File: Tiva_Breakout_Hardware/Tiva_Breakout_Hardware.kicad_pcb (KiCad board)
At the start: 2 copper layers, 146.1 x 69.8 mm, 15 parts, among them U1 TM4C129E_Launchpad

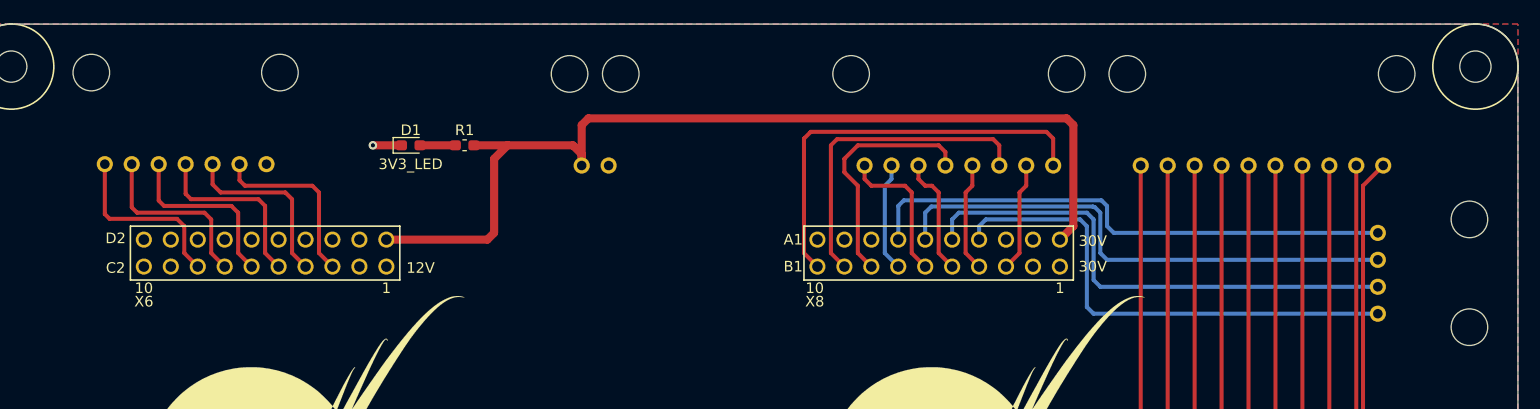
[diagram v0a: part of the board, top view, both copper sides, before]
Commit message: Finished 30V LEDs and connectors
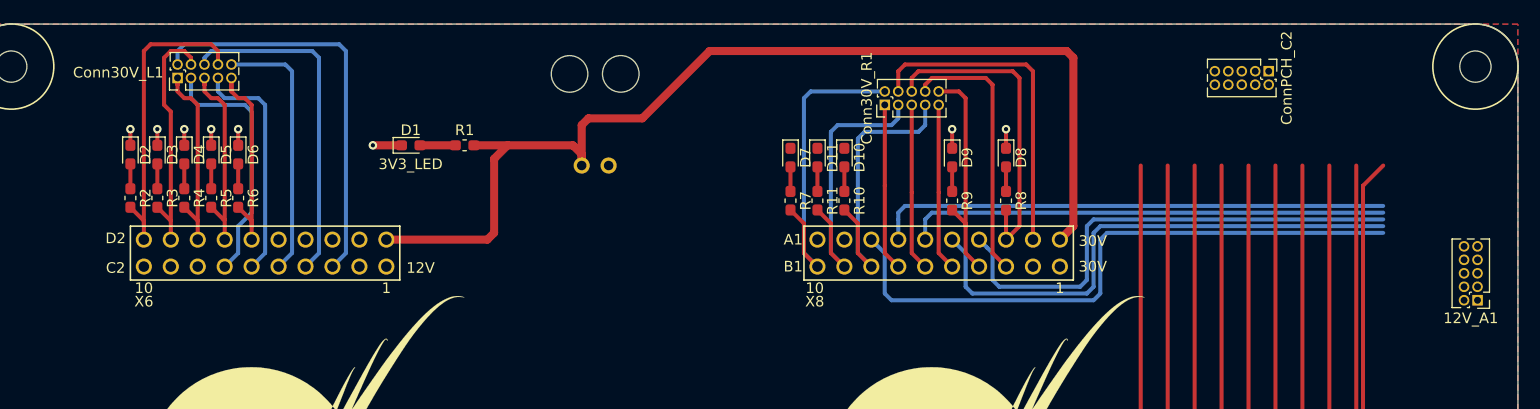
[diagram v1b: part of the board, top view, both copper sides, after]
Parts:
- removed 12V_B2: Molex_SL_04, MRDT_Connectors:MOLEX_SL_04_Horizontal
- added 12V_A1: PH_2x5, Connector_PinHeader_1.27mm:PinHeader_2x05_P1.27mm_Vertical, F.Cu at (226.8, 101.3)
- added D10: 3V3_LED, LED_SMD:LED_0603_1608Metric_Pad1.05x0.95mm_HandSolder, F.Cu at (167.1, 87.9)
- added D11: 3V3_LED, LED_SMD:LED_0603_1608Metric_Pad1.05x0.95mm_HandSolder, F.Cu at (164.5, 87.9)
- added D2: 3V3_LED, LED_SMD:LED_0603_1608Metric_Pad1.05x0.95mm_HandSolder, F.Cu at (99.8, 87.6)
- added D3: 3V3_LED, LED_SMD:LED_0603_1608Metric_Pad1.05x0.95mm_HandSolder, F.Cu at (102.3, 87.6)
- added D4: 3V3_LED, LED_SMD:LED_0603_1608Metric_Pad1.05x0.95mm_HandSolder, F.Cu at (104.9, 87.6)
- added D5: 3V3_LED, LED_SMD:LED_0603_1608Metric_Pad1.05x0.95mm_HandSolder, F.Cu at (107.4, 87.6)
- added D6: 3V3_LED, LED_SMD:LED_0603_1608Metric_Pad1.05x0.95mm_HandSolder, F.Cu at (109.9, 87.6)
- added D7: 3V3_LED, LED_SMD:LED_0603_1608Metric_Pad1.05x0.95mm_HandSolder, F.Cu at (162.0, 87.9)
- added D8: 3V3_LED, LED_SMD:LED_0603_1608Metric_Pad1.05x0.95mm_HandSolder, F.Cu at (182.3, 87.9)
- added D9: 3V3_LED, LED_SMD:LED_0603_1608Metric_Pad1.05x0.95mm_HandSolder, F.Cu at (177.2, 87.9)
- added R10: 330, Resistor_SMD:R_0603_1608Metric_Pad1.05x0.95mm_HandSolder, F.Cu at (167.1, 92.0)
- added R11: 330, Resistor_SMD:R_0603_1608Metric_Pad1.05x0.95mm_HandSolder, F.Cu at (164.5, 92.0)
- added R2: 330, Resistor_SMD:R_0603_1608Metric_Pad1.05x0.95mm_HandSolder, F.Cu at (99.8, 91.7)
- added R3: 330, Resistor_SMD:R_0603_1608Metric_Pad1.05x0.95mm_HandSolder, F.Cu at (102.3, 91.7)
- added R4: 330, Resistor_SMD:R_0603_1608Metric_Pad1.05x0.95mm_HandSolder, F.Cu at (104.9, 91.7)
- added R5: 330, Resistor_SMD:R_0603_1608Metric_Pad1.05x0.95mm_HandSolder, F.Cu at (107.4, 91.7)
- added R6: 330, Resistor_SMD:R_0603_1608Metric_Pad1.05x0.95mm_HandSolder, F.Cu at (109.9, 91.7)
- added R7: 330, Resistor_SMD:R_0603_1608Metric_Pad1.05x0.95mm_HandSolder, F.Cu at (162.0, 92.0)
- added R8: 330, Resistor_SMD:R_0603_1608Metric_Pad1.05x0.95mm_HandSolder, F.Cu at (182.3, 92.0)
- added R9: 330, Resistor_SMD:R_0603_1608Metric_Pad1.05x0.95mm_HandSolder, F.Cu at (177.2, 92.0)
- Conn30V_L1: value Molex_SL_07 -> PH_2x5; footprint MRDT_Connectors:MOLEX_SL_07_Horizontal -> Connector_PinHeader_1.27mm:PinHeader_2x05_P1.27mm_Vertical; moved to F.Cu
- Conn30V_R1: value Molex_SL_08 -> PH_2x5; footprint MRDT_Connectors:MOLEX_SL_08_Horizontal -> Connector_PinHeader_1.27mm:PinHeader_2x05_P1.27mm_Vertical; moved to F.Cu
- ConnPCH_C2: value Molex_SL_10 -> PH_2x5; footprint MRDT_Connectors:MOLEX_SL_10_Horizontal -> Connector_PinHeader_1.27mm:PinHeader_2x05_P1.27mm_Vertical; moved to F.Cu
- moved Conn30V_R1 9.03 mm to (170.9, 82.9), turned to 90 degrees
- moved ConnPCH_C2 8.91 mm to (207.1, 79.8), turned to 270 degrees
- moved Conn30V_L1 8.16 mm to (104.2, 80.4), turned to 90 degrees
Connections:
- net 12V_ON renamed M6_EN
- net Net-(Conn30V_L1-Pad2) renamed M3_ISENSE
- Conn30V_L1 pad 1: Net-(Conn30V_L1-Pad1) -> M3_EN
- Conn30V_L1 pad 3: Net-(Conn30V_L1-Pad3) -> M4_ISENSE
- Conn30V_L1 pad 4: Net-(Conn30V_L1-Pad4) -> M2_EN
- Conn30V_L1 pad 5: Net-(Conn30V_L1-Pad5) -> M4_EN
- Conn30V_L1 pad 6: Net-(Conn30V_L1-Pad6) -> M2_ISENSE
- Conn30V_L1 pad 7: Net-(Conn30V_L1-Pad7) -> M5_ISENSE
- Conn30V_R1 pad 1: EX_ON -> M6_ISENSE
- Conn30V_R1 pad 2: EX_CURR -> RKT_EN
- Conn30V_R1 pad 4: 12V_CURR -> RKT_ISENSE
- Conn30V_R1 pad 5: AUX_ON -> SP_ISENSE
- Conn30V_R1 pad 6: AUX_CURR -> AUX_EN
- Conn30V_R1 pad 7: RKT_ON -> SP_EN
- Conn30V_R1 pad 8: RKT_CURR -> AUX_ISENSE
- U1 pad PA6: AUX_ON -> SP_EN
- U1 pad PB5: Net-(Conn30V_L1-Pad3) -> M2_ISENSE
- U1 pad PC4: Net-(U1-PadPC4) -> AUX_EN
- U1 pad PD5: Net-(U1-PadPD5) -> M5_EN
- U1 pad PD7: RKT_ON -> M6_ISENSE
- U1 pad PE0: EX_CURR -> AUX_ISENSE
- U1 pad PE1: 12V_CURR -> 12V_EN
- U1 pad PE2: AUX_CURR -> 12V_ISENSE
- U1 pad PE3: RKT_CURR -> SP_ISENSE
- U1 pad PE4: Net-(U1-PadPE4) -> RKT_ISENSE
- U1 pad PF1: Net-(ConnPCH_C2-Pad1) -> Net-(U1-PadPF1)
- U1 pad PF2: Net-(ConnPCH_C2-Pad2) -> Net-(U1-PadPF2)
- U1 pad PF3: Net-(ConnPCH_C2-Pad3) -> Net-(U1-PadPF3)
- U1 pad PG0: Net-(ConnPCH_C2-Pad4) -> Net-(U1-PadPG0)
- U1 pad PK0: Net-(Conn30V_L1-Pad4) -> M1_ISENSE
- U1 pad PK1: Net-(Conn30V_L1-Pad5) -> M5_ISENSE
- U1 pad PK2: Net-(Conn30V_L1-Pad6) -> M4_ISENSE
- U1 pad PK3: Net-(Conn30V_L1-Pad7) -> Net-(U1-PadPK3)
- U1 pad PL0: Net-(ConnPCH_C2-Pad7) -> Net-(U1-PadPL0)
- U1 pad PL1: Net-(ConnPCH_C2-Pad8) -> Net-(U1-PadPL1)
- U1 pad PL2: Net-(ConnPCH_C2-Pad9) -> Net-(U1-PadPL2)
- U1 pad PL3: Net-(ConnPCH_C2-Pad10) -> Net-(U1-PadPL3)
- U1 pad PL4: Net-(ConnPCH_C2-Pad5) -> Net-(U1-PadPL4)
- U1 pad PL5: Net-(ConnPCH_C2-Pad6) -> Net-(U1-PadPL5)
- U1 pad PM5: EX_ON -> RKT_EN
- U1 pad PN4: Net-(U1-PadPN4) -> M1_EN
- U1 pad PN5: Net-(U1-PadPN5) -> M2_EN
- U1 pad PP4: Net-(U1-PadPP4) -> M3_EN
- U1 pad PQ0: Net-(U1-PadPQ0) -> M4_EN
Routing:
- net Net-(U1-PadPL3): track 0.00 -> 79.9 mm
- net Net-(U1-PadPL2): track 0.00 -> 79.9 mm
- net Net-(U1-PadPL0): track 0.00 -> 79.9 mm
- net Net-(U1-PadPG0): track 0.00 -> 79.9 mm
- net Net-(U1-PadPF3): track 0.00 -> 79.9 mm
- net Net-(ConnPCH_C2-Pad9): track 79.9 -> 0.00 mm
- net Net-(ConnPCH_C2-Pad7): track 79.9 -> 0.00 mm
- net Net-(ConnPCH_C2-Pad4): track 79.9 -> 0.00 mm
- net Net-(ConnPCH_C2-Pad3): track 79.9 -> 0.00 mm
- net Net-(ConnPCH_C2-Pad10): track 79.9 -> 0.00 mm
- net Net-(U1-PadPL5): track 0.00 -> 79.9 mm
- net Net-(U1-PadPL4): track 0.00 -> 79.9 mm
- net Net-(U1-PadPL1): track 0.00 -> 79.9 mm
- net Net-(ConnPCH_C2-Pad8): track 79.9 -> 0.00 mm
- net Net-(ConnPCH_C2-Pad6): track 79.9 -> 0.00 mm
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
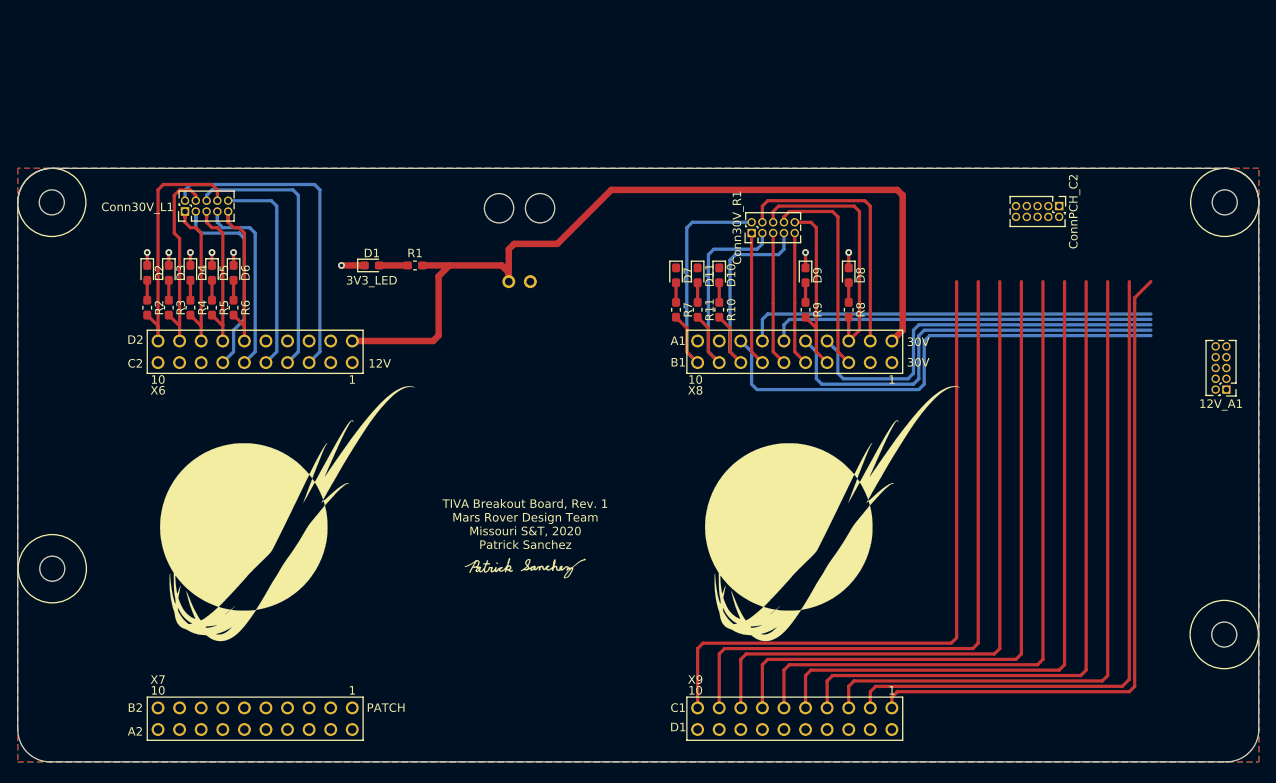
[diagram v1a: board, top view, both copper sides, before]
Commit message: Rerouted 30V for readability; routed 12V and LEDs
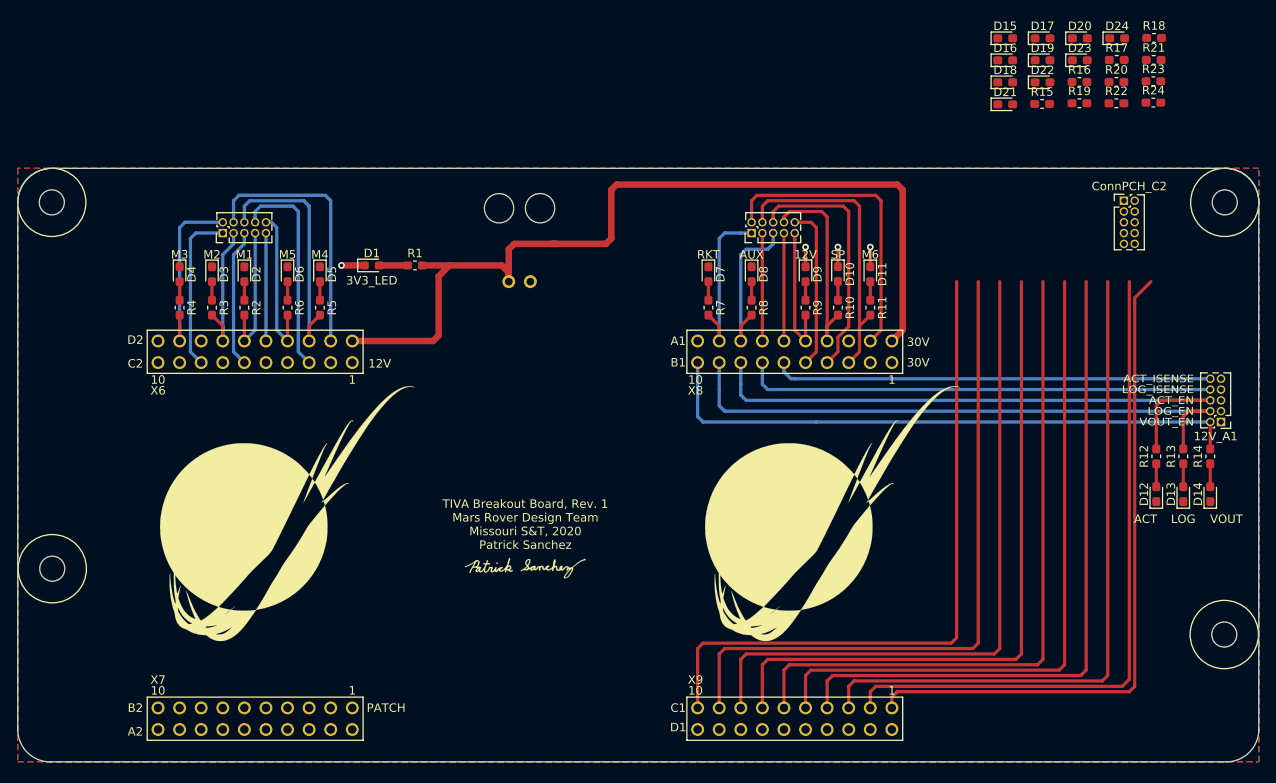
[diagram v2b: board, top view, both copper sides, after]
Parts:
- added D12: 3V3_LED, LED_SMD:LED_0603_1608Metric_Pad1.05x0.95mm_HandSolder, F.Cu at (218.5, 113.7)
- added D13: 3V3_LED, LED_SMD:LED_0603_1608Metric_Pad1.05x0.95mm_HandSolder, F.Cu at (221.7, 113.7)
- added D14: 3V3_LED, LED_SMD:LED_0603_1608Metric_Pad1.05x0.95mm_HandSolder, F.Cu at (224.9, 113.7)
- added D15: 3V3_LED, LED_SMD:LED_0603_1608Metric_Pad1.05x0.95mm_HandSolder, F.Cu at (200.7, 60.0)
- added D16: 3V3_LED, LED_SMD:LED_0603_1608Metric_Pad1.05x0.95mm_HandSolder, F.Cu at (200.7, 62.6)
- added D17: 3V3_LED, LED_SMD:LED_0603_1608Metric_Pad1.05x0.95mm_HandSolder, F.Cu at (205.1, 60.0)
- added D18: 3V3_LED, LED_SMD:LED_0603_1608Metric_Pad1.05x0.95mm_HandSolder, F.Cu at (200.7, 65.2)
- added D19: 3V3_LED, LED_SMD:LED_0603_1608Metric_Pad1.05x0.95mm_HandSolder, F.Cu at (205.1, 62.6)
- added D20: 3V3_LED, LED_SMD:LED_0603_1608Metric_Pad1.05x0.95mm_HandSolder, F.Cu at (209.5, 60.0)
- added D21: 3V3_LED, LED_SMD:LED_0603_1608Metric_Pad1.05x0.95mm_HandSolder, F.Cu at (200.7, 67.8)
- added D22: 3V3_LED, LED_SMD:LED_0603_1608Metric_Pad1.05x0.95mm_HandSolder, F.Cu at (205.1, 65.2)
- added D23: 3V3_LED, LED_SMD:LED_0603_1608Metric_Pad1.05x0.95mm_HandSolder, F.Cu at (209.5, 62.6)
- added D24: 3V3_LED, LED_SMD:LED_0603_1608Metric_Pad1.05x0.95mm_HandSolder, F.Cu at (213.9, 60.0)
- added R12: 330, Resistor_SMD:R_0603_1608Metric_Pad1.05x0.95mm_HandSolder, F.Cu at (218.5, 109.2)
- added R13: 330, Resistor_SMD:R_0603_1608Metric_Pad1.05x0.95mm_HandSolder, F.Cu at (221.7, 109.2)
- added R14: 330, Resistor_SMD:R_0603_1608Metric_Pad1.05x0.95mm_HandSolder, F.Cu at (224.9, 109.2)
- added R15: 330, Resistor_SMD:R_0603_1608Metric_Pad1.05x0.95mm_HandSolder, F.Cu at (205.1, 67.7)
- added R16: 330, Resistor_SMD:R_0603_1608Metric_Pad1.05x0.95mm_HandSolder, F.Cu at (209.5, 65.1)
- added R17: 330, Resistor_SMD:R_0603_1608Metric_Pad1.05x0.95mm_HandSolder, F.Cu at (213.9, 62.6)
- added R18: 330, Resistor_SMD:R_0603_1608Metric_Pad1.05x0.95mm_HandSolder, F.Cu at (218.3, 60.0)
- added R19: 330, Resistor_SMD:R_0603_1608Metric_Pad1.05x0.95mm_HandSolder, F.Cu at (209.5, 67.7)
- added R20: 330, Resistor_SMD:R_0603_1608Metric_Pad1.05x0.95mm_HandSolder, F.Cu at (213.8, 65.1)
- added R21: 330, Resistor_SMD:R_0603_1608Metric_Pad1.05x0.95mm_HandSolder, F.Cu at (218.2, 62.6)
- added R22: 330, Resistor_SMD:R_0603_1608Metric_Pad1.05x0.95mm_HandSolder, F.Cu at (213.8, 67.7)
- added R23: 330, Resistor_SMD:R_0603_1608Metric_Pad1.05x0.95mm_HandSolder, F.Cu at (218.2, 65.1)
- added R24: 330, Resistor_SMD:R_0603_1608Metric_Pad1.05x0.95mm_HandSolder, F.Cu at (218.2, 67.6)
- moved R11 20.3 mm to (184.9, 91.7)
- moved D11 20.3 mm to (184.9, 87.8)
- moved R10 14.0 mm to (181.1, 91.7)
- moved D10 14.0 mm to (181.1, 87.8)
- moved D5 12.7 mm to (120.1, 87.8)
- moved R5 12.7 mm to (120.1, 91.7)
- moved R8 11.4 mm to (170.9, 91.7)
- moved D2 11.4 mm to (111.2, 87.8)
- moved D8 11.4 mm to (170.9, 87.8)
- moved R2 11.4 mm to (111.2, 91.7)
- moved ConnPCH_C2 7.65 mm to (214.7, 79.1), turned to 0 degrees
- moved D6 6.35 mm to (116.3, 87.8)
- moved R6 6.35 mm to (116.3, 91.7)
- moved Conn30V_L1 5.12 mm to (108.7, 82.9)
- moved D3 5.08 mm to (107.4, 87.8)
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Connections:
- 12V_A1 pad 1: Net-(12V_A1-Pad1) -> GND
- 12V_A1 pad 10: Net-(12V_A1-Pad10) -> ACT_ISENSE
- 12V_A1 pad 2: Net-(12V_A1-Pad2) -> VOUT_EN
- 12V_A1 pad 3: Net-(12V_A1-Pad3) -> GND
- 12V_A1 pad 4: Net-(12V_A1-Pad4) -> LOG_EN
- 12V_A1 pad 5: Net-(12V_A1-Pad5) -> GND
- 12V_A1 pad 6: Net-(12V_A1-Pad6) -> ACT_EN
- 12V_A1 pad 7: Net-(12V_A1-Pad7) -> GND
- 12V_A1 pad 8: Net-(12V_A1-Pad8) -> LOG_ISENSE
- 12V_A1 pad 9: Net-(12V_A1-Pad9) -> GND
- Conn30V_L1 pad 1: M3_EN -> M3_ISENSE
- Conn30V_L1 pad 10: M1_ISENSE -> M5_EN
- Conn30V_L1 pad 2: M3_ISENSE -> M3_EN
- Conn30V_L1 pad 3: M4_ISENSE -> M2_EN
- Conn30V_L1 pad 4: M2_EN -> M4_ISENSE
- Conn30V_L1 pad 5: M4_EN -> M2_ISENSE
- Conn30V_L1 pad 6: M2_ISENSE -> M4_EN
- Conn30V_L1 pad 7: M5_ISENSE -> M1_EN
- Conn30V_L1 pad 8: M1_EN -> M5_ISENSE
- Conn30V_L1 pad 9: M5_EN -> M1_ISENSE
- Conn30V_R1 pad 1: M6_ISENSE -> RKT_EN
- Conn30V_R1 pad 10: 12V_EN -> 12V_ISENSE
- Conn30V_R1 pad 2: RKT_EN -> M6_ISENSE
- Conn30V_R1 pad 3: M6_EN -> RKT_ISENSE
- Conn30V_R1 pad 4: RKT_ISENSE -> M6_EN
- Conn30V_R1 pad 5: SP_ISENSE -> AUX_EN
- Conn30V_R1 pad 6: AUX_EN -> SP_ISENSE
- Conn30V_R1 pad 7: SP_EN -> AUX_ISENSE
- Conn30V_R1 pad 8: AUX_ISENSE -> SP_EN
- Conn30V_R1 pad 9: 12V_ISENSE -> 12V_EN
- ConnPCH_C2 pad 1: Net-(ConnPCH_C2-Pad1) -> PATCH10_EN
- ConnPCH_C2 pad 10: Net-(ConnPCH_C2-Pad10) -> PATCH5_EN
- ConnPCH_C2 pad 2: Net-(ConnPCH_C2-Pad2) -> PATCH1_EN
- ConnPCH_C2 pad 3: Net-(ConnPCH_C2-Pad3) -> PATCH9_EN
- ConnPCH_C2 pad 4: Net-(ConnPCH_C2-Pad4) -> PATCH2_EN
- ConnPCH_C2 pad 5: Net-(ConnPCH_C2-Pad5) -> PATCH8_EN
- ConnPCH_C2 pad 6: Net-(ConnPCH_C2-Pad6) -> PATCH3_EN
- ConnPCH_C2 pad 7: Net-(ConnPCH_C2-Pad7) -> PATCH7_EN
- ConnPCH_C2 pad 8: Net-(ConnPCH_C2-Pad8) -> PATCH4_EN
- ConnPCH_C2 pad 9: Net-(ConnPCH_C2-Pad9) -> PATCH6_EN
- U1 pad PA6: SP_EN -> ACT_EN
- U1 pad PB2: Net-(U1-PadPB2) -> RKT_EN
- U1 pad PB4: M3_ISENSE -> M5_ISENSE
- U1 pad PB5: M2_ISENSE -> Net-(U1-PadPB5)
- U1 pad PC4: AUX_EN -> Net-(U1-PadPC4)
- U1 pad PC5: Net-(U1-PadPC5) -> SP_EN
- U1 pad PC6: Net-(U1-PadPC6) -> 12V_EN
- U1 pad PC7: Net-(U1-PadPC7) -> AUX_EN
- U1 pad PD2: Net-(U1-PadPD2) -> M4_ISENSE
- U1 pad PD3: Net-(U1-PadPD3) -> RKT_ISENSE
- U1 pad PD4: Net-(U1-PadPD4) -> M1_ISENSE
- U1 pad PD5: M5_EN -> M1_EN
- U1 pad PD7: M6_ISENSE -> LOG_ISENSE
- U1 pad PE0: AUX_ISENSE -> M6_EN
- U1 pad PE1: 12V_EN -> SP_ISENSE
- U1 pad PE3: SP_ISENSE -> ACT_ISENSE
- U1 pad PE4: RKT_ISENSE -> M6_ISENSE
- U1 pad PE5: Net-(U1-PadPE5) -> AUX_ISENSE
- U1 pad PF1: Net-(U1-PadPF1) -> PATCH1_EN
- U1 pad PF2: Net-(U1-PadPF2) -> PATCH2_EN
- U1 pad PF3: Net-(U1-PadPF3) -> PATCH3_EN
- U1 pad PG0: Net-(U1-PadPG0) -> PATCH4_EN
- U1 pad PK0: M1_ISENSE -> Net-(U1-PadPK0)
- U1 pad PK1: M5_ISENSE -> M2_ISENSE
- U1 pad PK2: M4_ISENSE -> Net-(U1-PadPK2)
- U1 pad PK3: Net-(U1-PadPK3) -> M3_ISENSE
- U1 pad PL0: Net-(U1-PadPL0) -> PATCH7_EN
- U1 pad PL1: Net-(U1-PadPL1) -> PATCH8_EN
- U1 pad PL2: Net-(U1-PadPL2) -> PATCH9_EN
- U1 pad PL3: Net-(U1-PadPL3) -> PATCH10_EN
- U1 pad PL4: Net-(U1-PadPL4) -> PATCH5_EN
- U1 pad PL5: Net-(U1-PadPL5) -> PATCH6_EN
- U1 pad PM4: M6_EN -> LOG_EN
- U1 pad PM5: RKT_EN -> VOUT_EN
- U1 pad PN4: M1_EN -> Net-(U1-PadPN4)
- U1 pad PN5: M2_EN -> M3_EN
- U1 pad PP0: Net-(U1-PadPP0) -> M4_EN
- U1 pad PP1: Net-(U1-PadPP1) -> M5_EN
- U1 pad PP4: M3_EN -> Net-(U1-PadPP4)
- U1 pad PQ0: M4_EN -> M2_EN
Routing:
- net PATCH9_EN: track 0.00 -> 79.9 mm
- net PATCH7_EN: track 0.00 -> 79.9 mm
- net PATCH4_EN: track 0.00 -> 79.9 mm
- net PATCH3_EN: track 0.00 -> 79.9 mm
- net PATCH10_EN: track 0.00 -> 79.9 mm
- net Net-(U1-PadPL3): track 79.9 -> 0.00 mm
- net Net-(U1-PadPL2): track 79.9 -> 0.00 mm
- net Net-(U1-PadPL0): track 79.9 -> 0.00 mm
- net Net-(U1-PadPG0): track 79.9 -> 0.00 mm
- net Net-(U1-PadPF3): track 79.9 -> 0.00 mm
- net PATCH8_EN: track 0.00 -> 79.9 mm
- net PATCH6_EN: track 0.00 -> 79.9 mm
- net PATCH5_EN: track 0.00 -> 79.9 mm
- net Net-(U1-PadPL5): track 79.9 -> 0.00 mm
- net Net-(U1-PadPL4): track 79.9 -> 0.00 mm
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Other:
- board text added: "ACT"
- board text added: "ACT_EN"
- board text added: "ACT_ISENSE"
- board text added: "AUX"
- board text added: "LOG"
- board text added: "LOG_EN"
- board text added: "LOG_ISENSE"
- board text added: "M1"
- board text added: "M2"
- board text added: "M3"
- board text added: "M4"
- board text added: "M5"
- board text added: "M6"
- board text added: "RKT"
- board text added: "SP"
- board text added: "VOUT"
- board text added: "VOUT_EN"
- board text removed: "12V_CURR"
- board text removed: "12V_ON"
- board text removed: "30V_L"
- board text removed: "30V_R"
- board text removed: "AUX_CURR"
- board text removed: "AUX_ON"
- board text removed: "EX_CURR"
- board text removed: "EX_ON"
- board text removed: "M1_CURR"
- board text removed: "M1_ON"
- board text removed: "M2_CURR"
- board text removed: "M2_ON"
- board text removed: "M3_CURR"
- board text removed: "M3_ON"
- board text removed: "RKT_CURR"
- board text removed: "RKT_ON"
